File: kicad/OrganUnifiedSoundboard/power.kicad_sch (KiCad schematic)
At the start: 8 parts, among them J2 5VOut, J4 12V INPUT, J5 GND INPUT, J7 5VOut

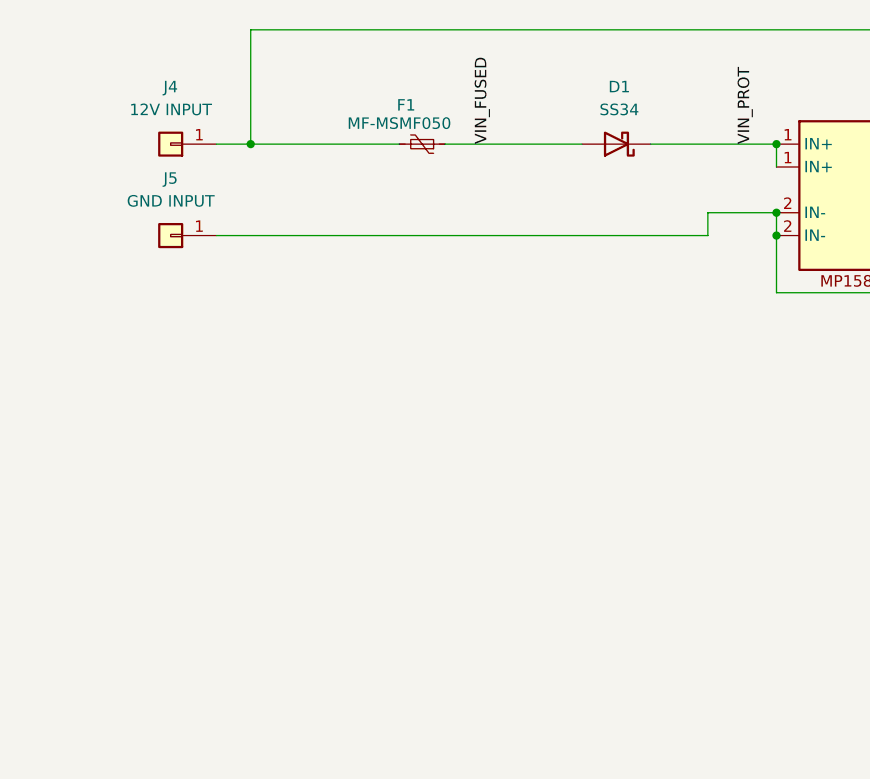
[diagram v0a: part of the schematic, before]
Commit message: Adding some custom components that some of the kicad things depend on
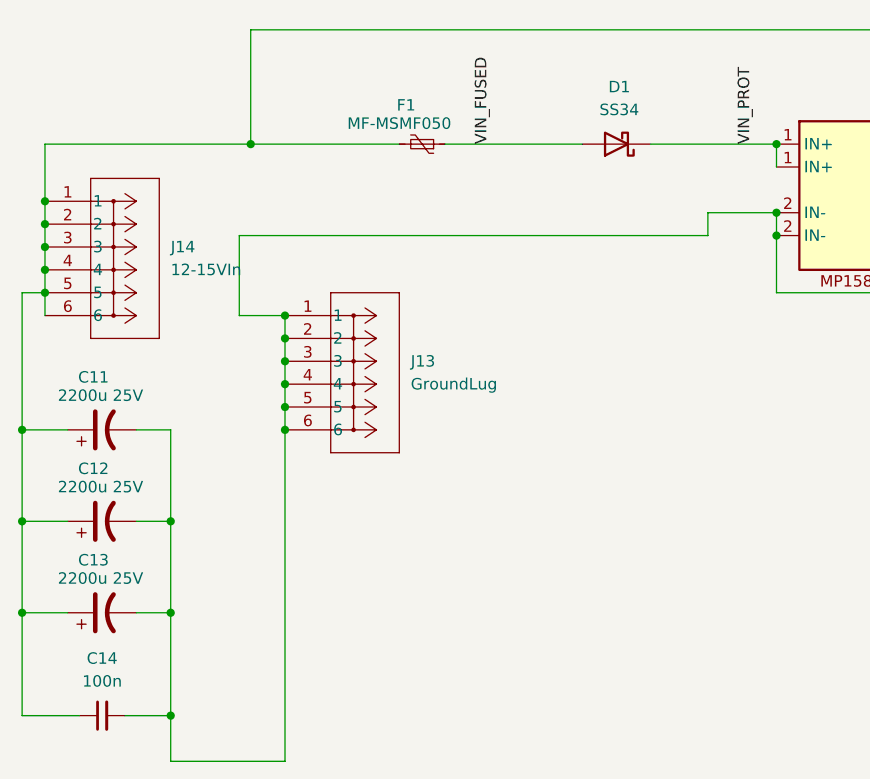
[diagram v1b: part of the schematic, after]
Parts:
- removed J4: 12V INPUT, symbol Connector_Generic:Conn_01x01
- removed J5: GND INPUT, symbol Connector_Generic:Conn_01x01
- added C11, C12, C13: 2200u 25V, Capacitor_THT:CP_Radial_D10.0mm_P5.00mm, symbol Device:C_Polarized_US
- added C14: 100n, Capacitor_SMD:C_0603_1608Metric, symbol Device:C_Small
- added J13: GroundLug, UL 8199:CONN_8199_KEY, symbol UL 8199:8199
- added J14: 12-15VIn, UL 8199:CONN_8199_KEY, symbol UL 8199:8199
- J2, J7: footprint (none) -> Connector_JST:JST_PH_B3B-PH-K_1x03_P2.00mm_Vertical
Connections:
- net 12V_out: now also C11.1, C12.1, C13.1, C14.1, J14.1, J14.2, J14.3, J14.4, J14.5, J14.6
- net GND_out: now also C11.2, C12.2, C13.2, C14.2, J13.1, J13.2, J13.3, J13.4, J13.5, J13.6

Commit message: Finalized unified soundboard driver for production, adding some models
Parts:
- added CR1: SMCJ24A, ul_smcj24a:SMCJSeries_LTF, symbol ul_smcj24a:SMCJ24A
- added J16: 12-15VOut, UL 8199:CONN_8199_KEY, symbol UL 8199:8199
- A5V1: footprint CustomLibrary:MP1584EN_Module -> CustomLibrary:MP1584_Module_simplified; symbol Custom_Library:MP1584 -> Custom_Library:MP1584_simplified
- J13: value GroundLug -> Ground
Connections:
- net GND_out: now also CR1.2
- net 12V_out: no longer names the net of C11.1, C12.1, C13.1, C14.1, F1.2, J14.1, J14.2, J14.3, J14.4, J14.5, J14.6
- net 12V_out: now also CR1.1, J16.1, J16.2, J16.3, J16.4, J16.5, J16.6
